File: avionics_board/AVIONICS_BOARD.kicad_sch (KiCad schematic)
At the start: 10 parts

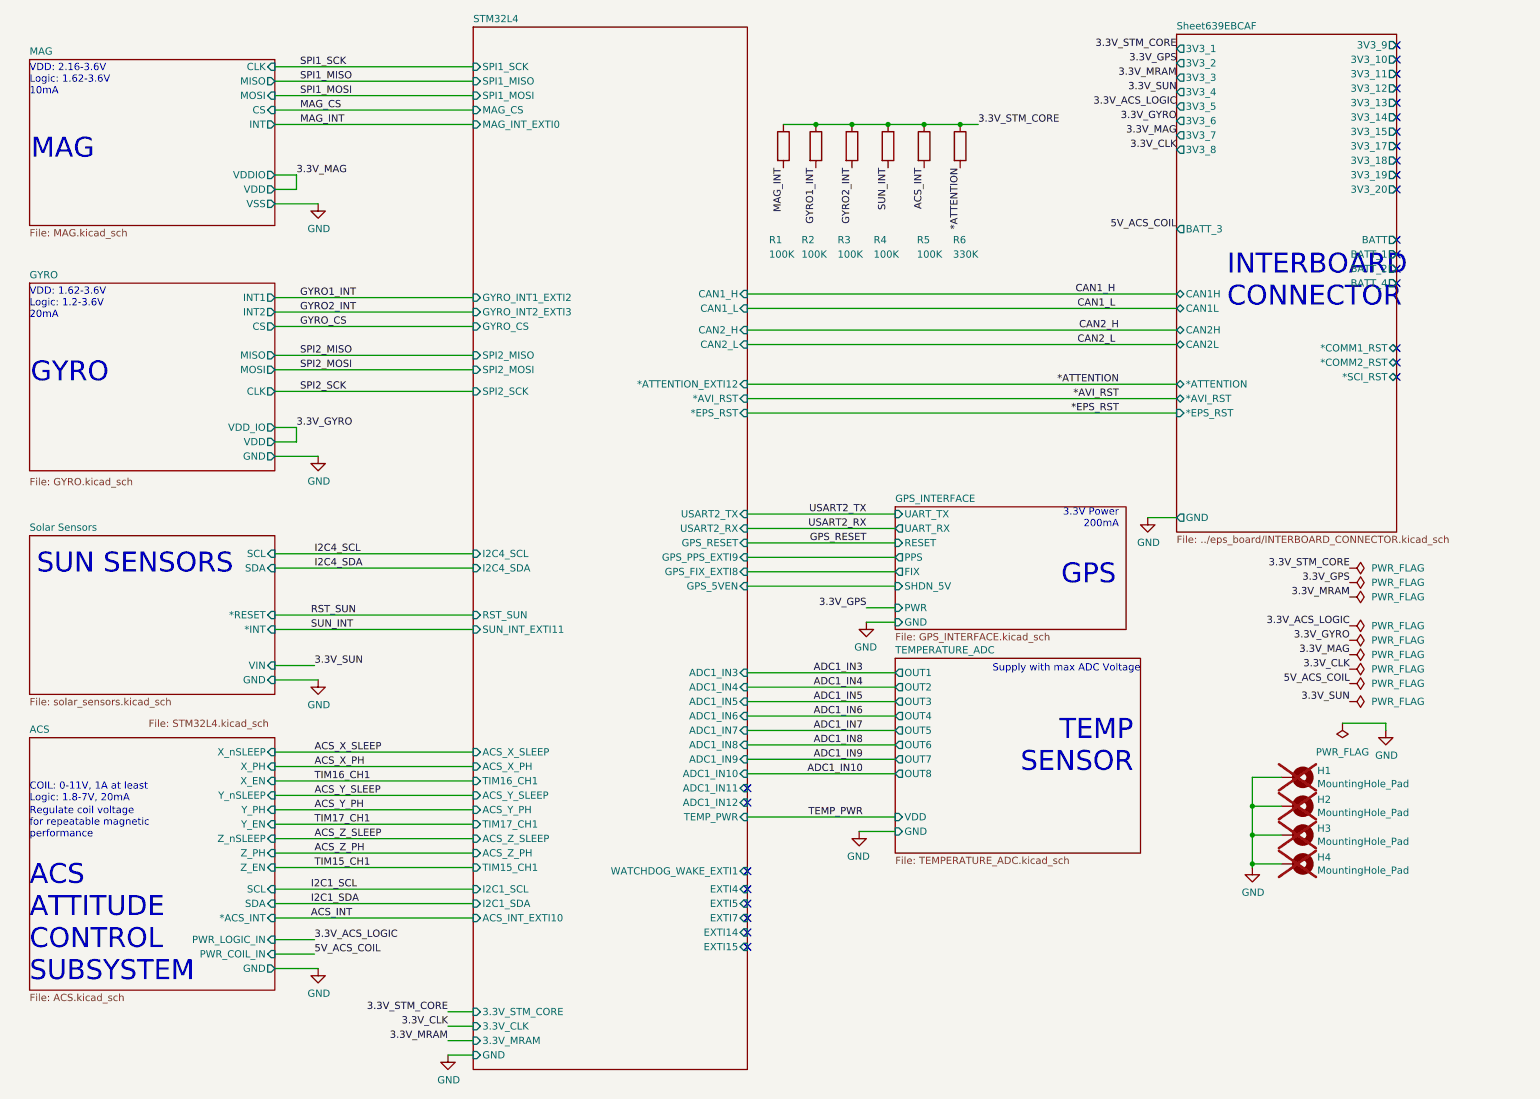
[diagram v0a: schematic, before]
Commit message: detailed power switches moved from EPS to invidual boards, each board only has core and aux bus (and batt if needed) which scales better. Reassign PC104 slots
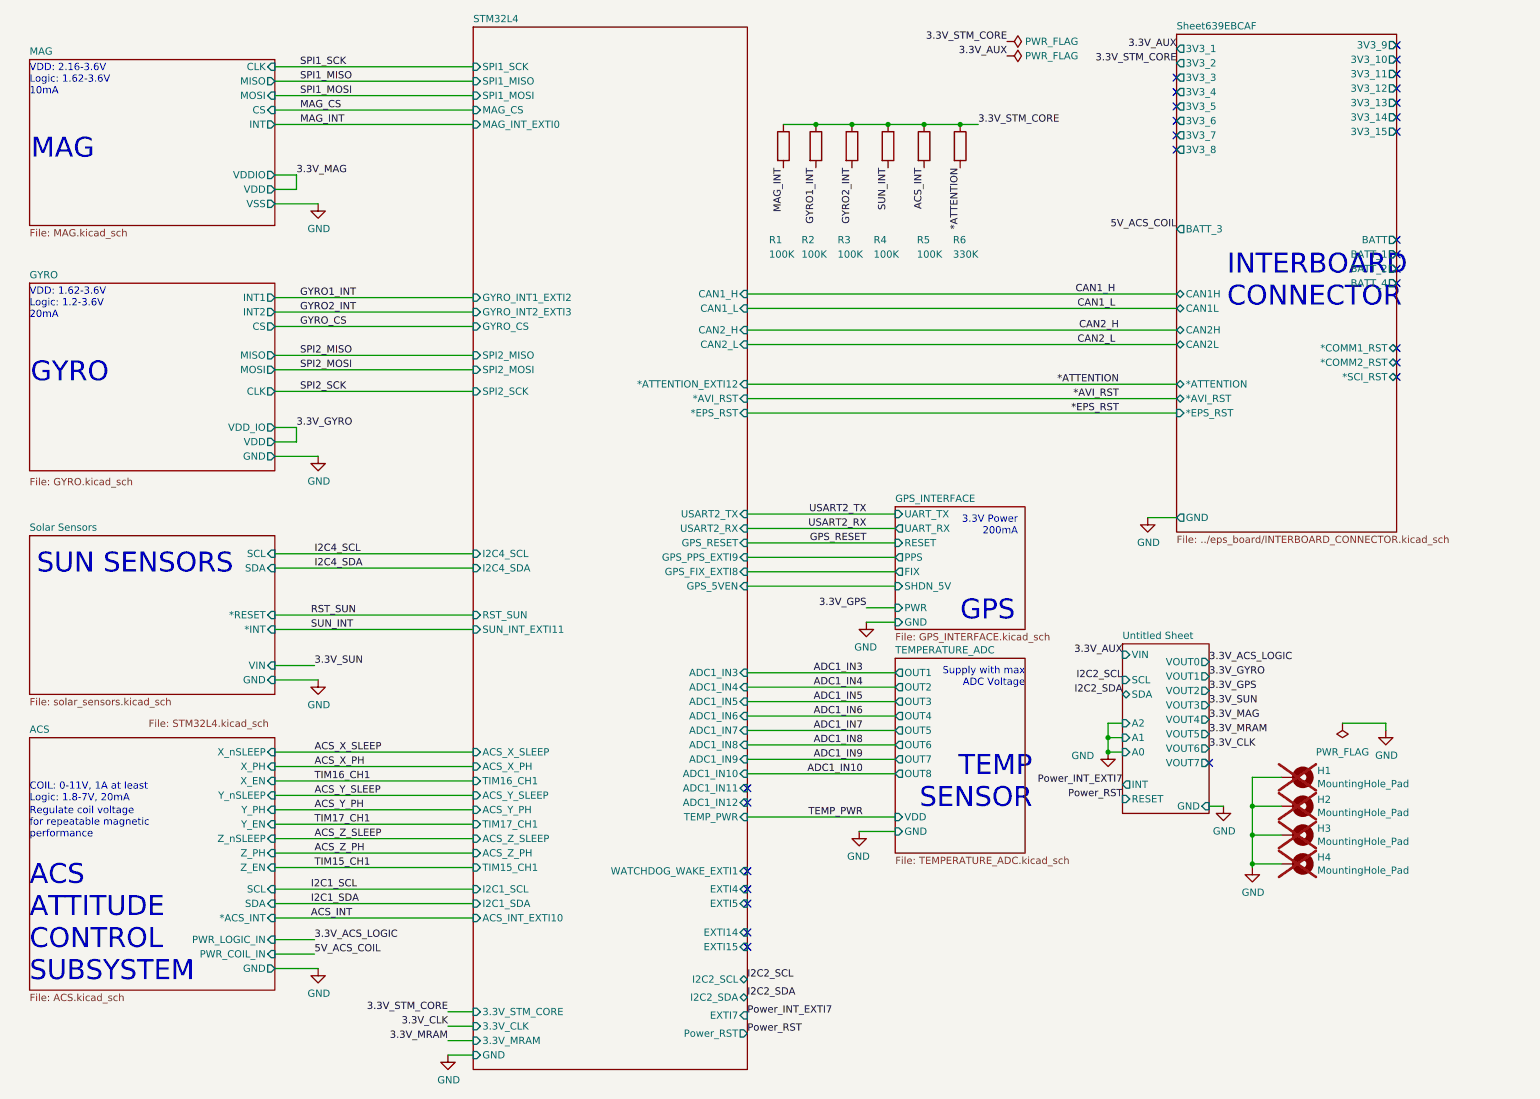
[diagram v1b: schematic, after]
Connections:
- no-connect marks 26 -> 28
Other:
- added sheet Untitled Sheet (../eps_board/i2c_power_switches_3v_sch.kicad_sch)
- sheet STM32L4 ports: added I2C2_SCL, I2C2_SDA, Power_RST; removed none
- sheet Sheet639EBCAF ports: added none; removed 3V3_17, 3V3_18, 3V3_19, 3V3_20

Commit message: AVI board simplified and cleaned up
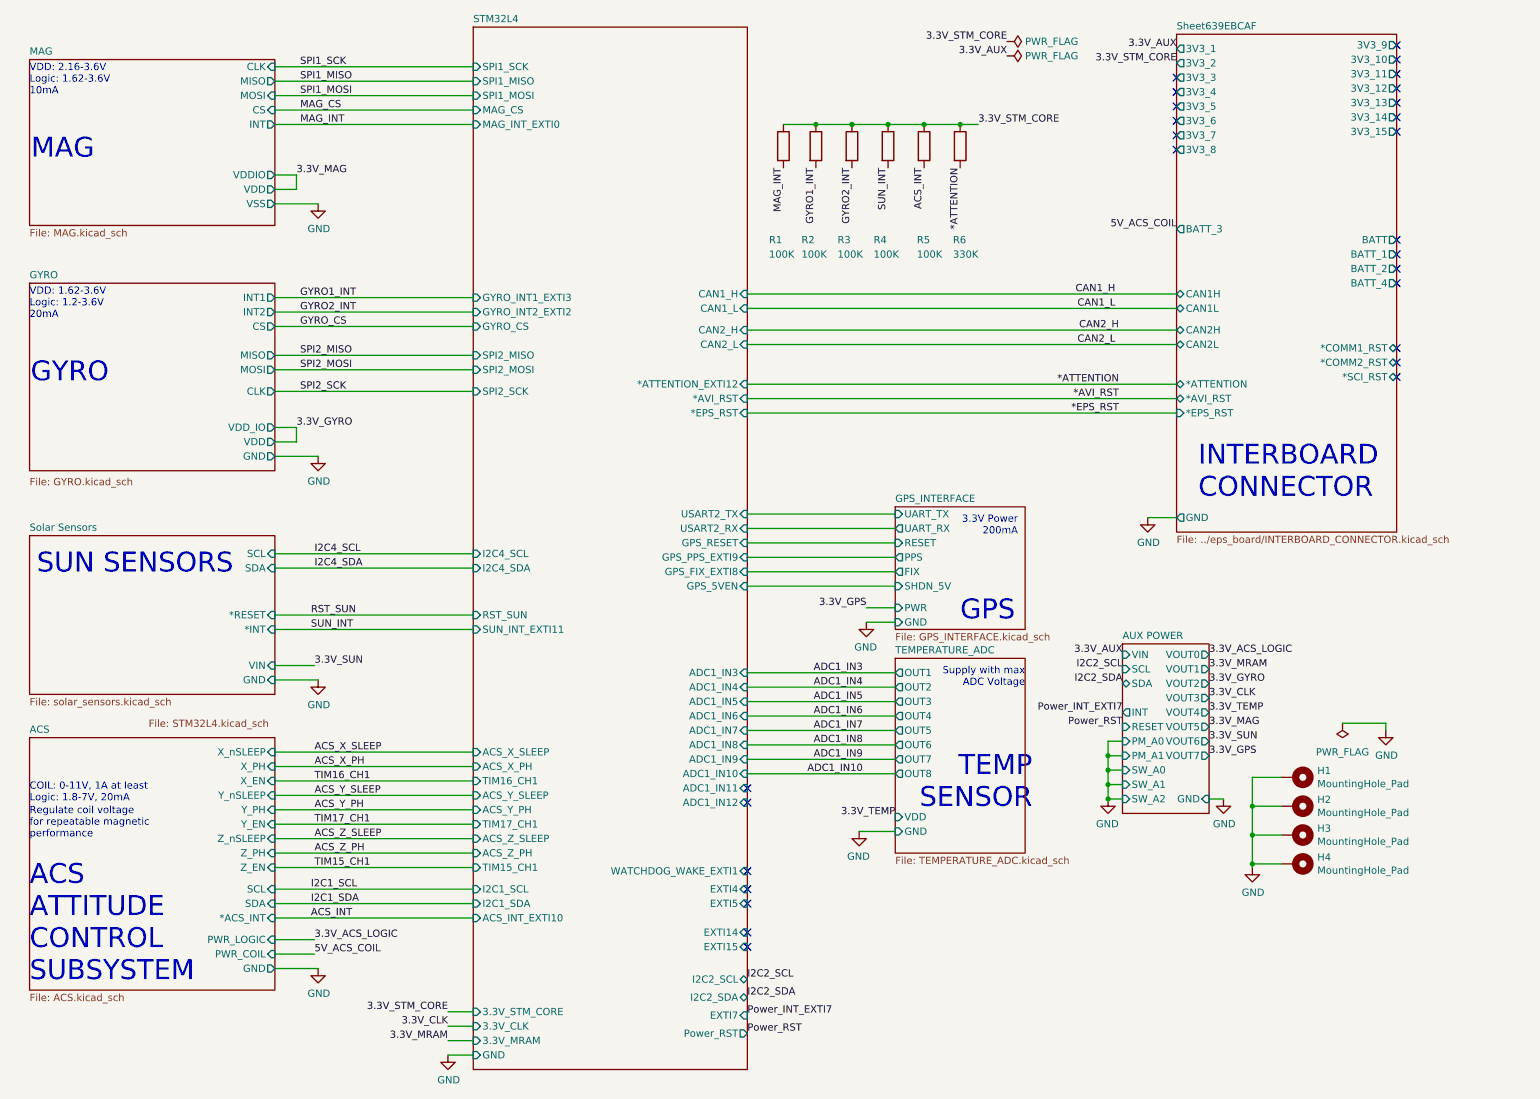
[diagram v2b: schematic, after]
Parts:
- H1, H2, H3, H4: now fitted; now left out of the parts list
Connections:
- no-connect marks 28 -> 27
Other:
- sheet Untitled Sheet renamed AUX POWER
- sheet ACS ports: added PWR_COIL, PWR_LOGIC; removed PWR_COIL_IN, PWR_LOGIC_IN
- sheet AUX POWER ports: added PM_A0, PM_A1, SW_A0, SW_A1, SW_A2; removed A0, A1, A2
- sheet STM32L4 ports: added GYRO_INT1_EXTI3, GYRO_INT2_EXTI2; removed GYRO_INT1_EXTI2, GYRO_INT2_EXTI3, TEMP_PWR

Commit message: EPS and AVI joint cleanup
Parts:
- added R11, R12, R21: 22, Resistor_SMD:R_0402_1005Metric_Pad0.72x0.64mm_HandSolder, symbol Device:R
- added R22, R46, R47: 22R, Resistor_SMD:R_0402_1005Metric_Pad0.72x0.64mm_HandSolder, symbol Device:R
- added R23, R24, R37, R38, R44, R45: 5K1, Resistor_SMD:R_0402_1005Metric_Pad0.72x0.64mm_HandSolder, symbol Device:R
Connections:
- net 3.3V_ACS_LOGIC: now also R23.1, R24.1
- net 3.3V_AUX: now also R44.1, R45.1
- net 3.3V_SUN: now also R37.1, R38.1
- net I2C1_SCL: now also R24.2
- net I2C1_SDA: now also R23.2
- net I2C2_SCL: now also R45.2
- net I2C2_SDA: now also R44.2
- net I2C4_SCL: now also R37.2
- net I2C4_SDA: now also R38.2
- net SPI1_MISO: now also R21.1
- net SPI1_MOSI: now also R12.1
- net SPI1_SCK: now also R11.1
- net SPI2_MISO: now also R22.1
- net SPI2_MOSI: now also R46.1
- net SPI2_SCK: now also R47.1
- new net STM32L4/SPI1_MISO: R21.2
- new net STM32L4/SPI1_MOSI: R12.2
- new net STM32L4/SPI1_SCK: R11.2
- new net STM32L4/SPI2_MISO: R22.2
- new net STM32L4/SPI2_MOSI: R46.2
- new net STM32L4/SPI2_SCK: R47.2
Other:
- sheet AUX POWER ports: added ENABLE_0, ENABLE_1, ENABLE_2, ENABLE_3, ENABLE_4, ENABLE_5, ENABLE_6, ENABLE_7, ENABLE_A, ENABLE_B, ENABLE_C, ENABLE_D, ENABLE_E, ENABLE_F, ENABLE_G, ENABLE_H, VOUT_A, VOUT_B, VOUT_C, VOUT_D, VOUT_E, VOUT_F, VOUT_G, VOUT_H; removed VOUT0, VOUT1, VOUT2, VOUT3, VOUT4, VOUT5, VOUT6, VOUT7

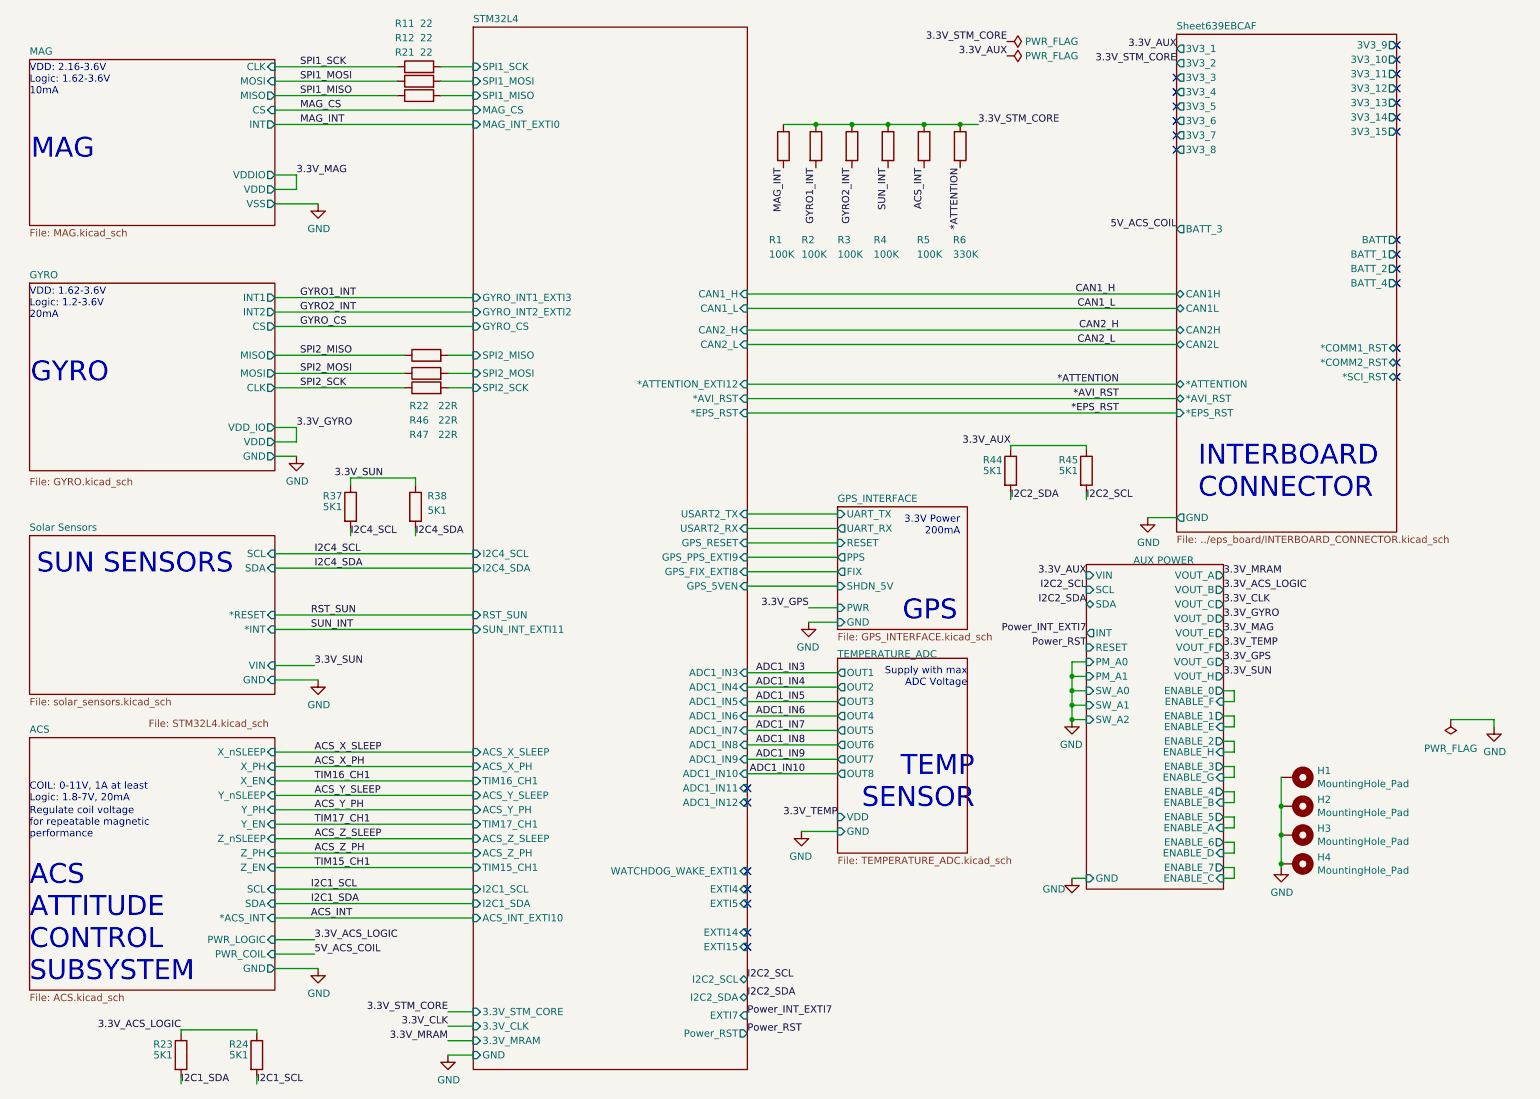
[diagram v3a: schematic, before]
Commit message: SCI AVI and EPS are now consistent
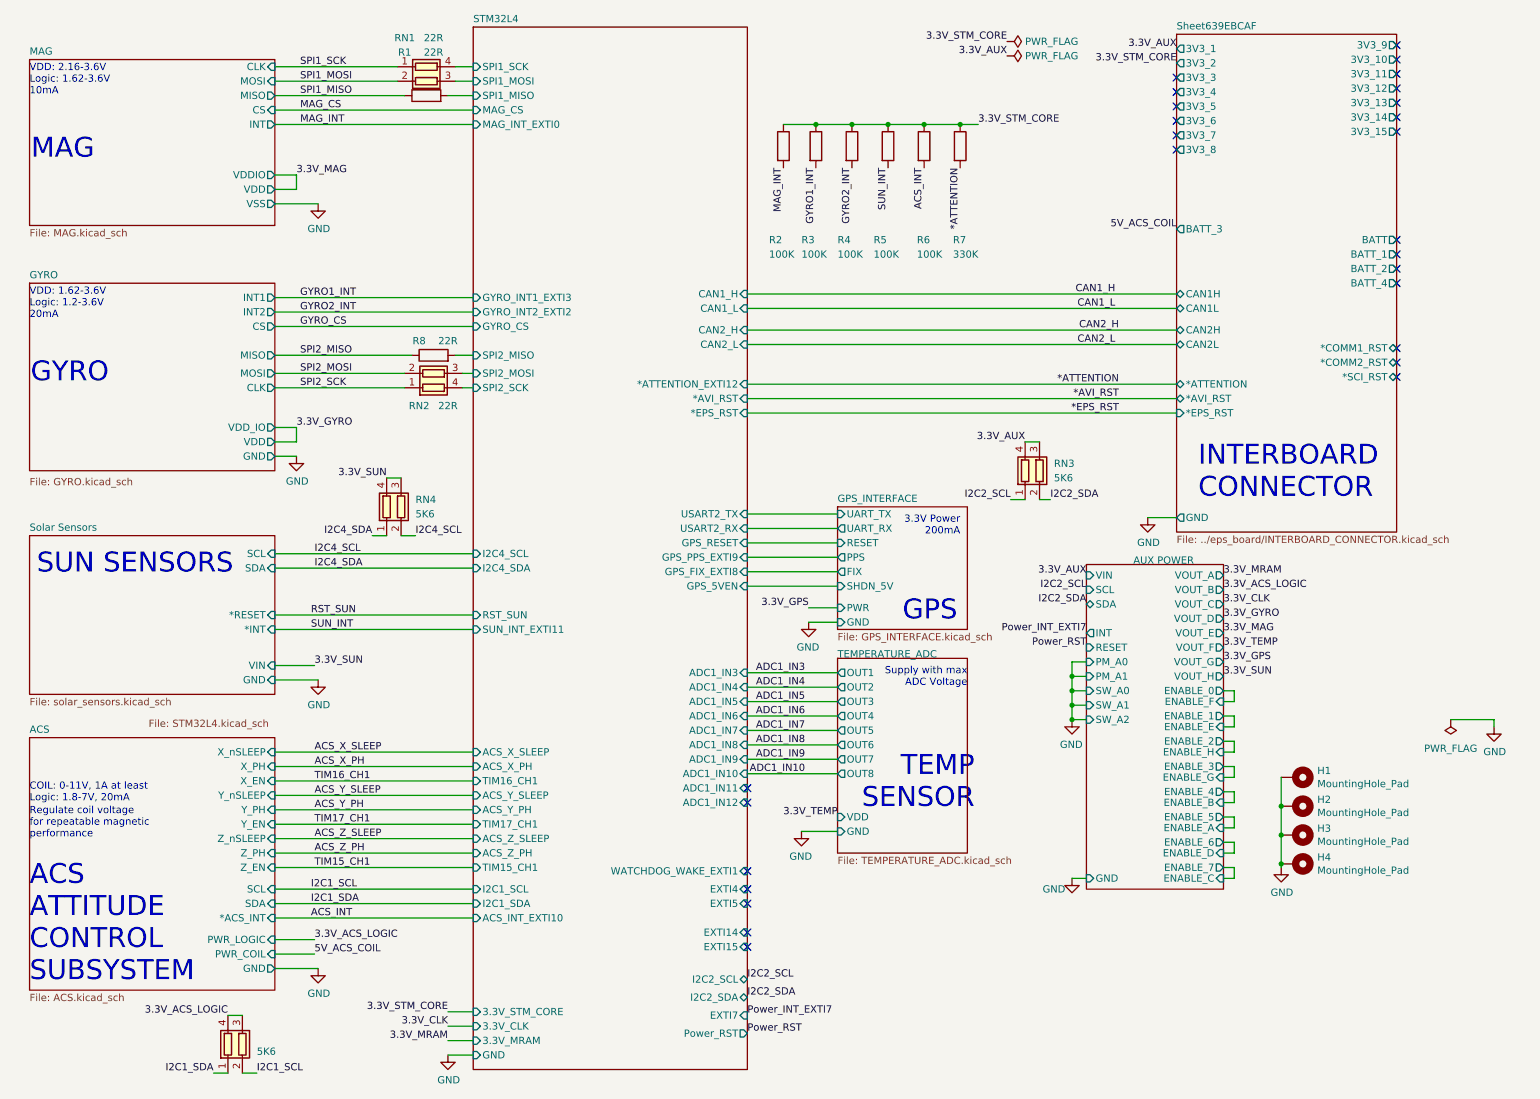
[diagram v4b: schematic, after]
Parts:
- removed R11, R12: 22, Resistor_SMD:R_0402_1005Metric_Pad0.72x0.64mm_HandSolder, symbol Device:R
- removed R23, R24, R37, R38, R44, R45: 5K1, Resistor_SMD:R_0402_1005Metric_Pad0.72x0.64mm_HandSolder, symbol Device:R
- removed R46, R47: 22R, Resistor_SMD:R_0402_1005Metric_Pad0.72x0.64mm_HandSolder, symbol Device:R
- added RN1, RN2: 22R, Resistor_SMD:R_Array_Convex_2x0402, symbol Device:R_Pack02
- added RN3, RN4, RN5: 5K6, Resistor_SMD:R_Array_Convex_2x0402, symbol Device:R_Pack02
- R1: renamed from R21; value 22 -> 22R
- renumbered R1 to R2, R2 to R3, R3 to R4, R4 to R5, R5 to R6, R6 to R7, R22 to R8
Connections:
- net 3.3V_ACS_LOGIC: now also RN5.3 (R2.2), RN5.4 (R1.2)
- net 3.3V_AUX: now also RN3.3 (R2.2), RN3.4 (R1.2)
- net 3.3V_SUN: now also RN4.3 (R2.2), RN4.4 (R1.2)
- net I2C1_SCL: now also RN5.2 (R2.1)
- net I2C1_SDA: now also RN5.1 (R1.1)
- net I2C2_SCL: now also RN3.1 (R1.1)
- net I2C2_SDA: now also RN3.2 (R2.1)
- net I2C4_SCL: now also RN4.2 (R2.1)
- net I2C4_SDA: now also RN4.1 (R1.1)
- net SPI1_MOSI: now also RN1.2 (R2.1)
- net SPI1_SCK: now also RN1.1 (R1.1)
- net SPI2_MOSI: now also RN2.2 (R2.1)
- net SPI2_SCK: now also RN2.1 (R1.1)
- net STM32L4/SPI1_MOSI: now also RN1.3 (R2.2)
- net STM32L4/SPI1_SCK: now also RN1.4 (R1.2)
- net STM32L4/SPI2_MOSI: now also RN2.3 (R2.2)
- net STM32L4/SPI2_SCK: now also RN2.4 (R1.2)
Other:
- moved on the sheet: R1, R8
